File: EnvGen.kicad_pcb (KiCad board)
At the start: 2 copper layers, 36 parts, among them J1 Input, J2 Output, J3 Power, Q1 BC817, Q2 BC817, Q3 BC817, U1 NE555, U2 LM324A

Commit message: copy from legacy repo
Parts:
- added J10: Conn_01x05_Male, footprint:pls1x05, B.Cu at (47.0, 78.0)
- added J11: Conn_01x05_Male, footprint:pls1x05, B.Cu at (72.4, 78.0)
- added J4: Conn_01x05_Male, footprint:pls1x05, B.Cu at (25.4, 24.0)
- added J5: Conn_01x05_Male, footprint:pls1x05, B.Cu at (25.4, 85.0)
- added J6: Conn_01x05_Male, footprint:pls1x05, B.Cu at (73.7, 24.0)
- added J7: Conn_01x05_Male, footprint:pls1x05, B.Cu at (77.7, 85.0)
- added J8: Conn_01x05_Male, footprint:pls1x05, B.Cu at (48.3, 85.0)
- added J9: Conn_01x05_Male, footprint:pls1x05, B.Cu at (24.1, 78.0)
- C1, C2, C4, C5, D1, D2, D3, D4, D5, D6, Q1, Q2, Q3, R1, R10, R12, R2, R3, R6, R7, R9, U1: moved to B.Cu
- J3: value Power -> Conn_01x05_Male; footprint footprint:pls1x03 -> footprint:pls1x05; moved to B.Cu
- R11, R13, R8: value R -> 100R; moved to B.Cu
- R4: value 10K -> 100R; moved to B.Cu
- R5: value 100R -> 10K; moved to B.Cu
- U2: value LM324A -> LM324; moved to B.Cu
- moved D1 127.9 mm to (37.1, 50.1)
- moved Q1 127.1 mm to (34.3, 60.6), turned to 270 degrees
- moved R10 123.5 mm to (44.0, 57.0)
- moved RV1 121.3 mm to (33.8, 40.9)
- moved J1 117.2 mm to (26.6, 55.5)
- moved D2 114.4 mm to (30.6, 55.5), turned to 180 degrees
- moved Q2 113.2 mm to (39.0, 60.5)
- moved R9 112.0 mm to (33.4, 56.2), turned to 90 degrees
- moved R4 107.8 mm to (40.5, 50.1), turned to 180 degrees
- moved D5 105.5 mm to (30.6, 58.1), turned to 180 degrees
- moved J3 105.5 mm to (48.3, 24.0), turned to 270 degrees
- moved C2 104.8 mm to (57.0, 59.6), turned to 90 degrees
- moved R12 104.4 mm to (42.0, 52.9)
- moved D3 103.2 mm to (38.8, 57.4), turned to 180 degrees
- moved R6 98.3 mm to (69.1, 69.7)
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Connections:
- C4 pad 1: GNDREF -> -5V
- C4 pad 2: +5V -> GNDREF
- C5 pad 1: -5V -> GNDREF
- C5 pad 2: GNDREF -> +5V
- J3 pad 1: +5V -> -5V
- J3 pad 2: GNDREF -> -5V
- R10 pad 2: Net-(D4-Pad2) -> Net-(D4-Pad1)
- R4 pad 1: +5V -> Net-(C3-Pad1)
- R4 pad 2: Net-(Q3-Pad3) -> Net-(D1-Pad2)
- R5 pad 1: Net-(C3-Pad1) -> +5V
- R5 pad 2: Net-(D1-Pad2) -> Net-(Q3-Pad3)
- RV2 pad 2: Net-(D4-Pad1) -> Net-(D4-Pad2)
- RV2 pad 3: Net-(D4-Pad1) -> Net-(D4-Pad2)
- U2 pad 11: (no net) -> +5V
- U2 pad 4: (no net) -> -5V
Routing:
- net GNDREF: track 0.00 -> 206.5 mm, vias 0 -> 5
- net -5V: track 0.00 -> 147.8 mm, vias 0 -> 1
- net +5V: track 0.00 -> 126.6 mm, vias 0 -> 4
- net Net-(C1-Pad2): track 0.00 -> 82.5 mm, vias 0 -> 4
- net Net-(C3-Pad1): track 0.00 -> 60.0 mm, vias 0 -> 5
- net Net-(Q1-Pad3): track 0.00 -> 57.9 mm, vias 0 -> 2
- net Net-(D6-Pad1): track 0.00 -> 57.1 mm
- net Net-(Q3-Pad3): track 0.00 -> 53.4 mm, vias 0 -> 2
- net Net-(C1-Pad1): track 0.00 -> 45.6 mm, vias 0 -> 2
- net Net-(R11-Pad1): track 0.00 -> 40.9 mm, vias 0 -> 2
- net Net-(Q2-Pad1): track 0.00 -> 39.5 mm, vias 0 -> 2
- net Net-(RV3-Pad3): track 0.00 -> 32.8 mm, vias 0 -> 1
- net Net-(RV2-Pad1): track 0.00 -> 29.1 mm
- net Net-(RV3-Pad2): track 0.00 -> 19.6 mm
- net Net-(D4-Pad1): track 0.00 -> 13.7 mm
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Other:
- board outline added: 80 x 70 mm
- net class power added: clearance 0.2, trace_width 0.5, via_dia 0.8, via_drill 0.4

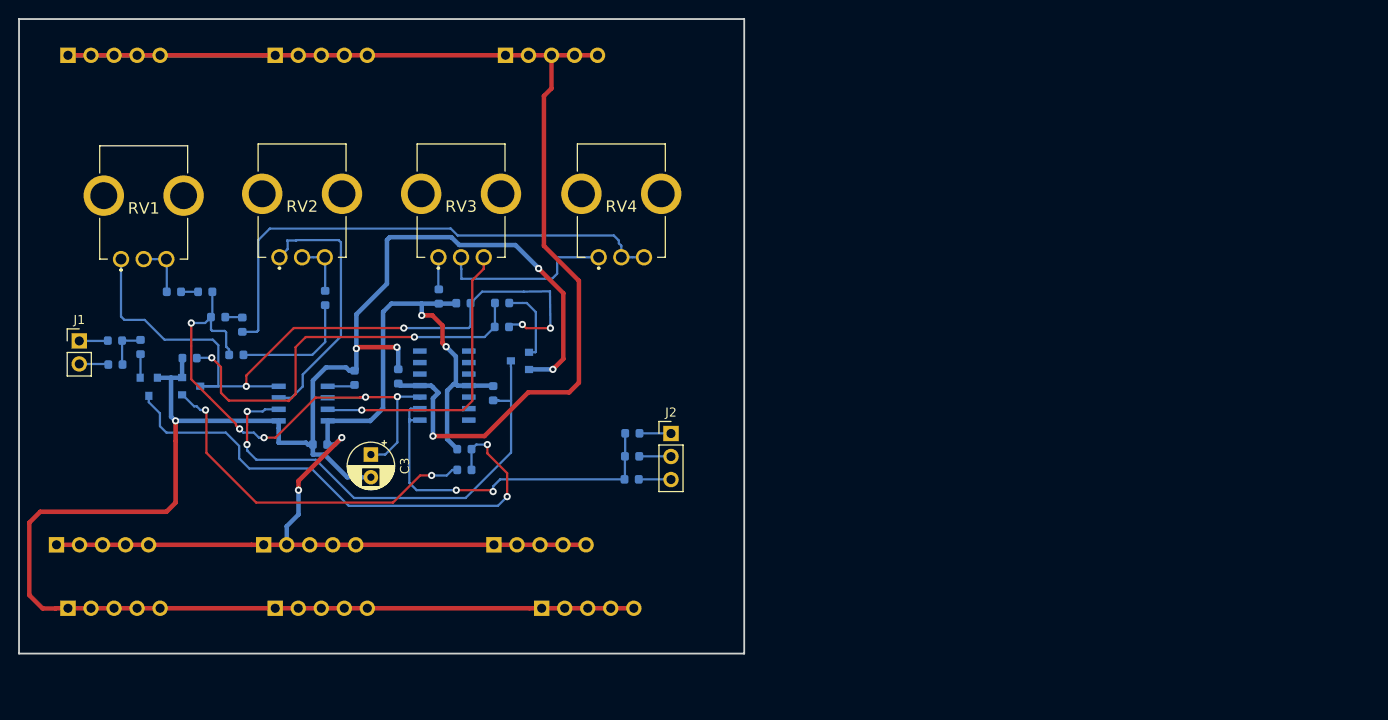
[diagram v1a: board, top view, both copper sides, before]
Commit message: Изменена плата до размера 40х70 мм
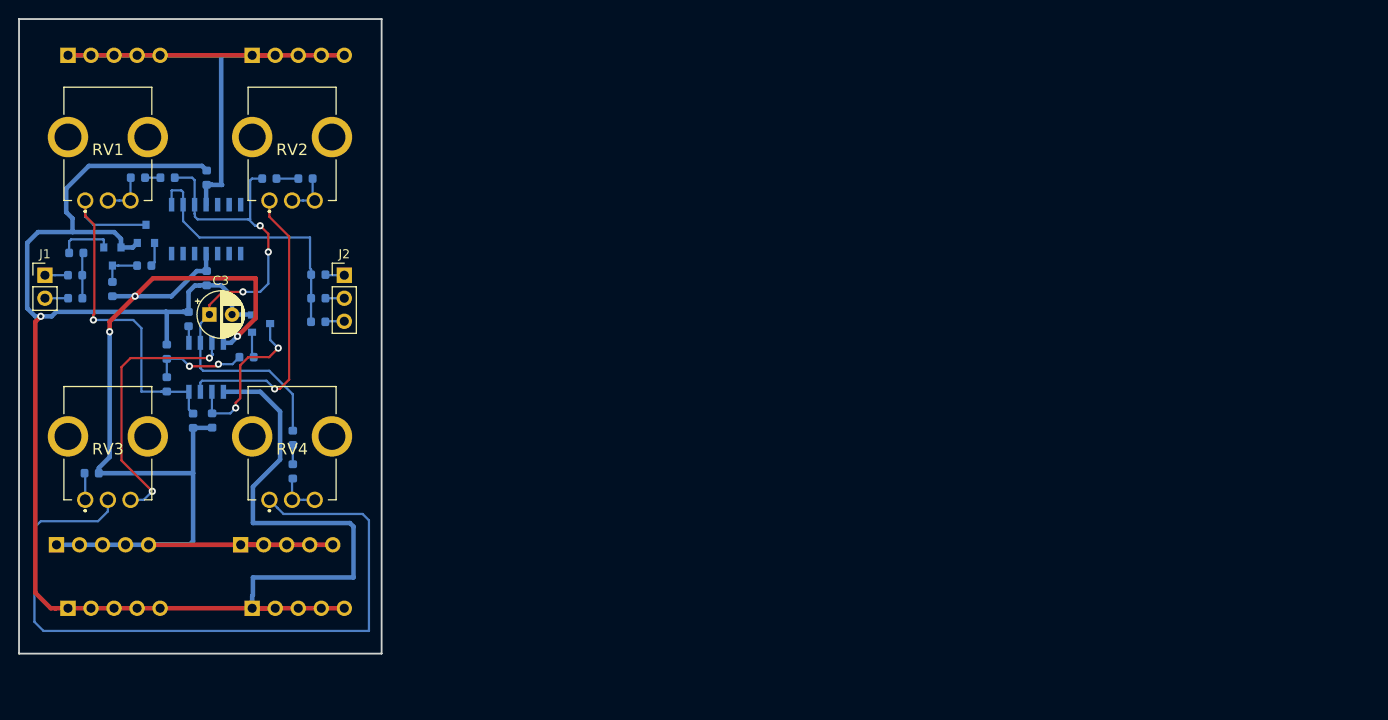
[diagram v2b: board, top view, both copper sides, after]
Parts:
- removed J11, J6, J7: Conn_01x05_Male, footprint:pls1x05
- moved RV3 47.3 mm to (29.8, 67.4)
- moved RV4 45.1 mm to (50.1, 67.4)
- moved R1 43.0 mm to (28.0, 70.1), turned to 0 degrees
- moved R2 42.7 mm to (30.3, 49.8), turned to 90 degrees
- moved R6 41.9 mm to (33.8, 47.2), turned to 180 degrees
- moved J2 40.1 mm to (55.9, 48.3)
- moved R8 38.8 mm to (53.0, 48.2)
- moved R11 38.8 mm to (53.0, 50.8)
- moved R13 38.7 mm to (53.0, 53.4)
- moved C1 37.5 mm to (36.3, 60.3), turned to 270 degrees
- moved R3 32.5 mm to (39.2, 64.3), turned to 90 degrees
- moved U2 31.4 mm to (40.6, 43.2), turned to 270 degrees
- moved R5 31.1 mm to (41.3, 64.3), turned to 90 degrees
- moved C4 30.5 mm to (40.7, 37.5)
- moved Q3 28.9 mm to (46.7, 53.6), turned to 0 degrees
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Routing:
- net -5V: track 147.8 -> 74.1 mm, vias 1 -> 0
- net Net-(RV3-Pad2): track 19.6 -> 81.9 mm
- net Net-(Q1-Pad3): track 57.9 -> 4.52 mm, vias 2 -> 0
- net Net-(D6-Pad1): track 57.1 -> 4.89 mm
- net Net-(C1-Pad2): track 82.5 -> 43.1 mm, vias 4 -> 1
- net Net-(Q2-Pad1): track 39.5 -> 2.64 mm, vias 2 -> 0
- net Net-(Q3-Pad3): track 53.4 -> 18.2 mm
- net Net-(C1-Pad1): track 45.6 -> 10.8 mm
- net +5V: track 126.6 -> 141.3 mm, vias 4 -> 3
- net Net-(D4-Pad1): track 13.7 -> 2.41 mm
- net Net-(R11-Pad1): track 40.9 -> 30.2 mm, vias 2 -> 0
- net GNDREF: track 206.5 -> 197.4 mm, vias 5 -> 1
- net Net-(Q3-Pad1): track 8.50 -> 2.98 mm
- net Net-(Q1-Pad1): track 2.61 -> 6.06 mm
- net Net-(RV2-Pad1): track 29.1 -> 32.4 mm, vias 0 -> 1
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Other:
- board size 80 x 70 mm -> 40 x 70 mm

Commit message: Изменены абсолютные пути к библиотекам и моделям на отнасительные. В схемах резисторы европейского УГО заменены на Российские
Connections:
- net GNDREF renamed GND

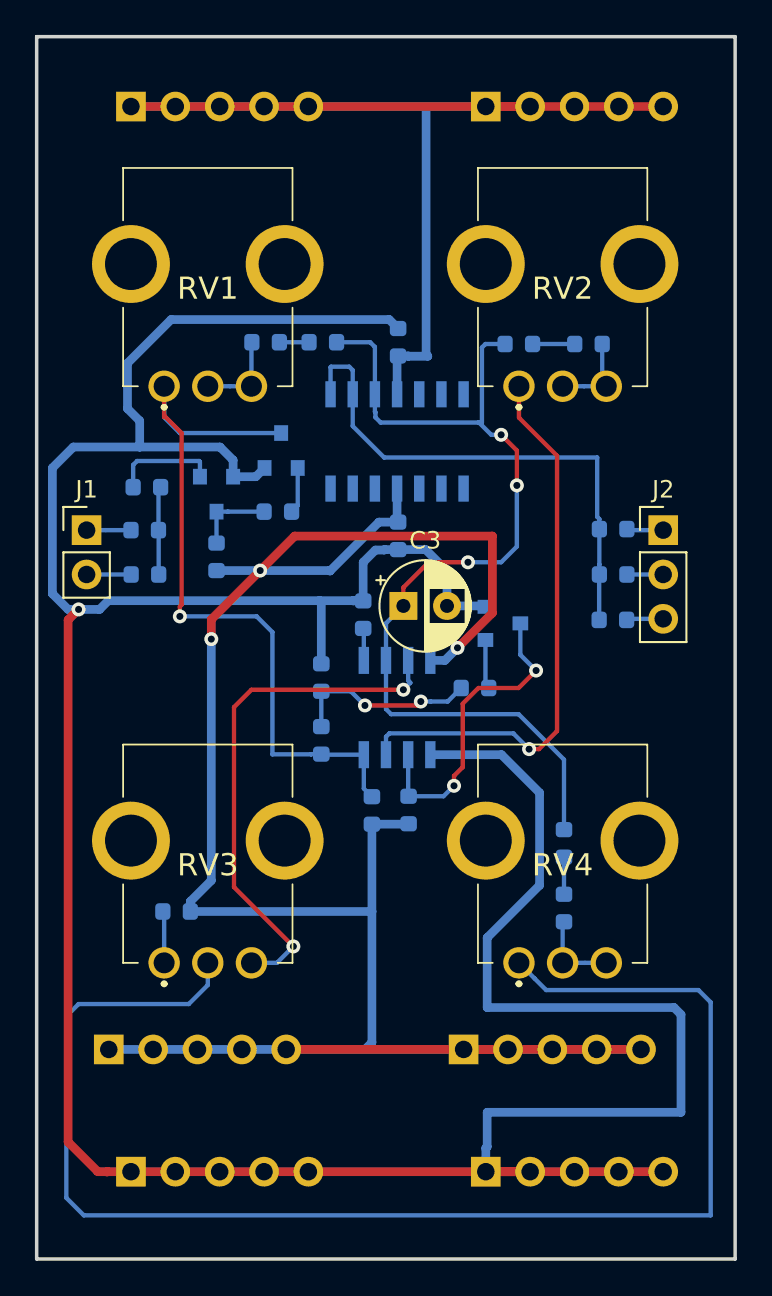
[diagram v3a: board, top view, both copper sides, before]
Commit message: Косметические изменения в схемах Плата 40х70 мм. Добавленны подписи компонентов и регуляторов  на плате
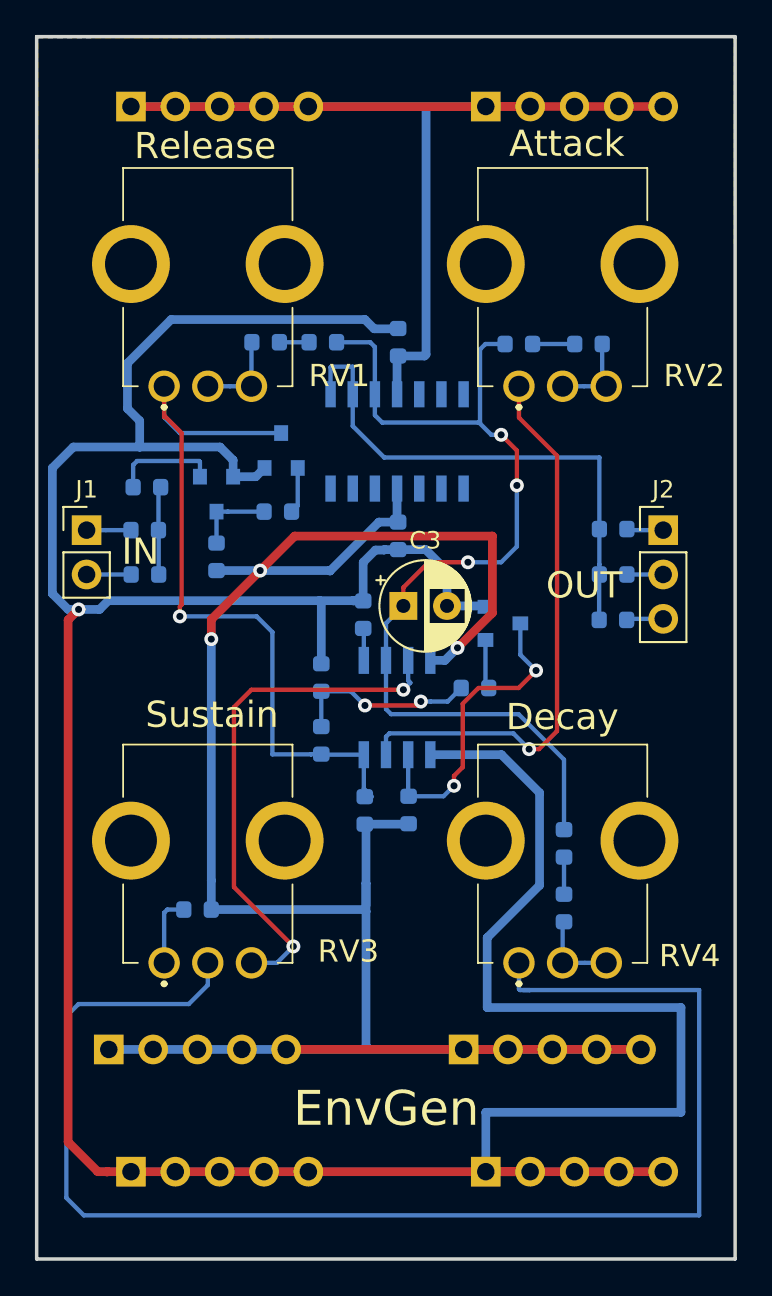
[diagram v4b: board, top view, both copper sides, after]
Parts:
- moved R1 1.21 mm to (29.2, 70.0)
- moved R3 0.41 mm to (38.8, 64.3)
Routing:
- net Net-(R1-Pad1): track 2.97 -> 4.07 mm
- net +5V: track 141.3 -> 140.7 mm
- added copper zone on B.Cu, net GND
- added copper zone on F.Cu, net GND
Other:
- board text added: "Attack"
- board text added: "Decay"
- board text added: "EnvGen"
- board text added: "IN"
- board text added: "OUT"
- board text added: "Release"
- board text added: "Sustain"
